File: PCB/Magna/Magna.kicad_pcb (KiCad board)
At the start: 2 copper layers, 100 x 100 mm, 136 parts, among them J702 Conn_ARM_SWD_TagConnect_TC2030, J703 Conn_ARM_JTAG_SWD_20, U1001 6N137, U1002 74HC08D, U201 24.576 MHz, U202 CY2305SXC-1HT, U203 CY2305SXC-1HT, U301 WM8782SEDS, U401 WM8782SEDS, U501 CS4344, U601 CS4344, U701 STM32F730V8T6, U802 USB3300-EZK, U901 AMS1117-5.0, U902 WS3222D, U903 TPS61040DBV, U904 XL1509-ADJ, Y701 24MHz

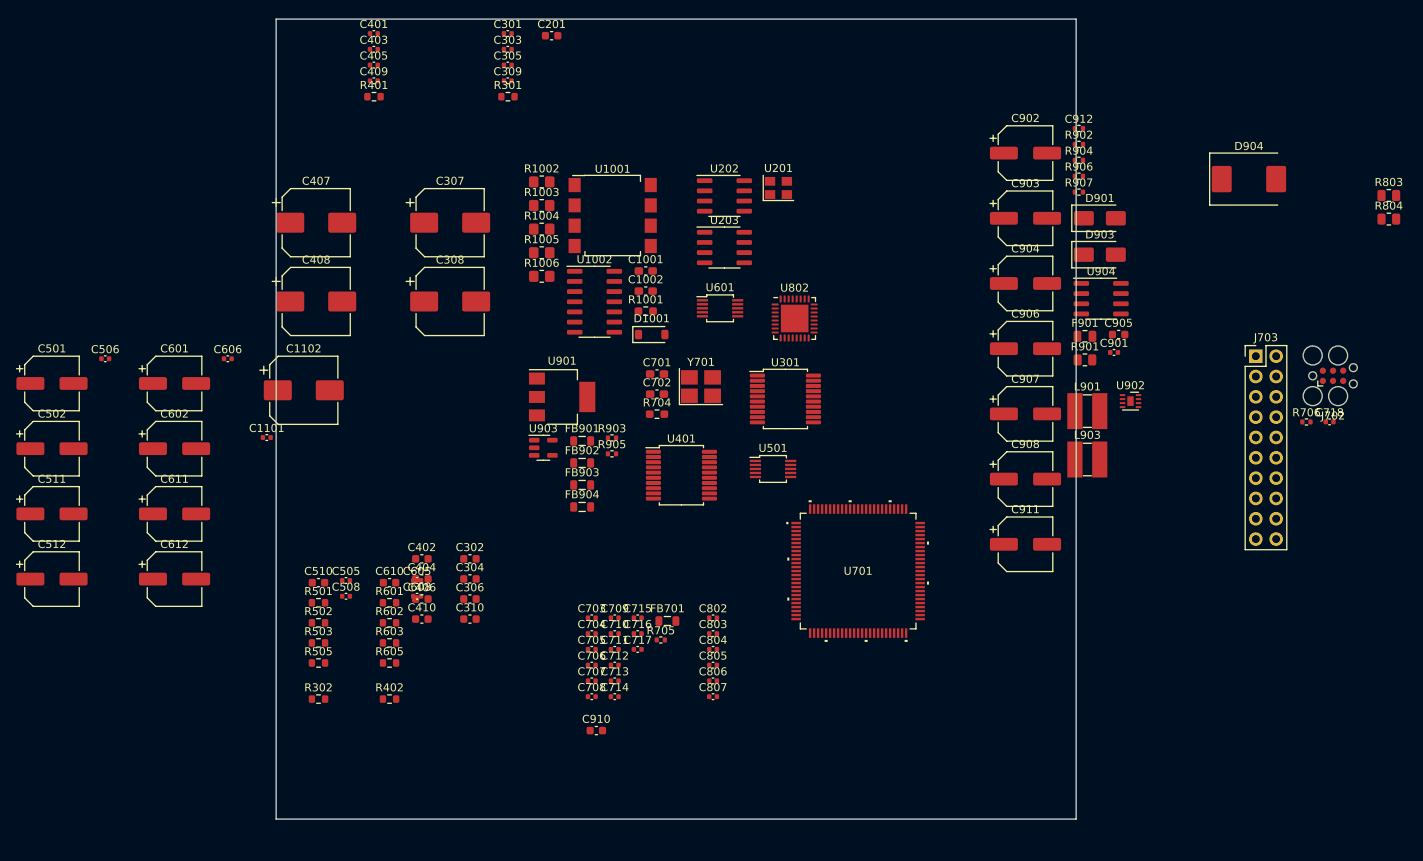
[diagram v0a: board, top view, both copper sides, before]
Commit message: Remove all ERC in schematics
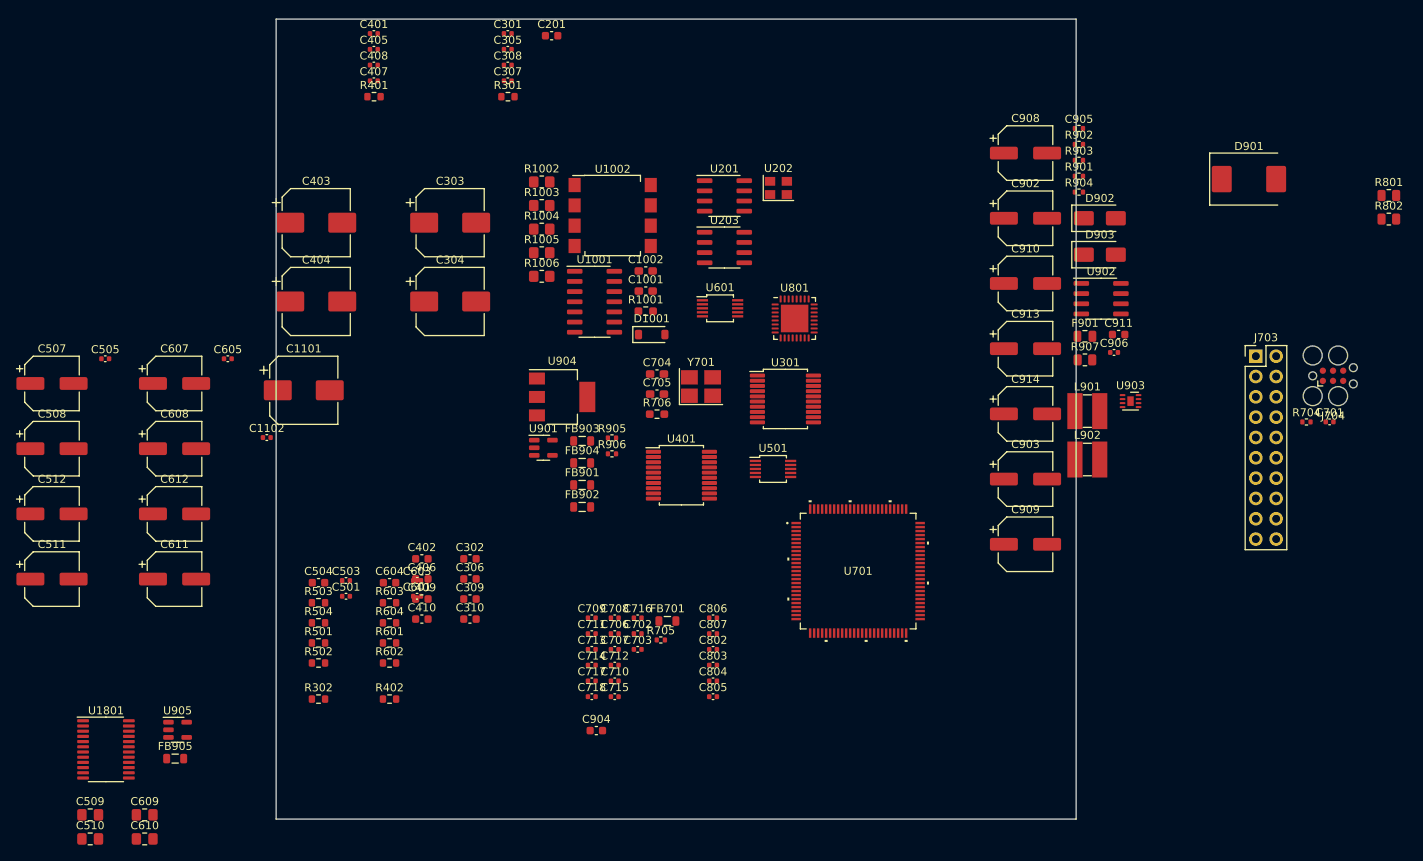
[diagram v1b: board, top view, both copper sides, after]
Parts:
- added C509: 10nF/50V, Capacitor_SMD:C_0805_2012Metric_Pad1.18x1.45mm_HandSolder, F.Cu at (46.8, 154.5)
- added C510: 10nF/50V, Capacitor_SMD:C_0805_2012Metric_Pad1.18x1.45mm_HandSolder, F.Cu at (46.8, 157.5)
- added C609: 10nF/50V, Capacitor_SMD:C_0805_2012Metric_Pad1.18x1.45mm_HandSolder, F.Cu at (53.6, 154.5)
- added C610: 10nF/50V, Capacitor_SMD:C_0805_2012Metric_Pad1.18x1.45mm_HandSolder, F.Cu at (53.6, 157.5)
- added FB905: FerriteBead, Inductor_SMD:L_0805_2012Metric, F.Cu at (57.4, 147.4)
- added U1801: XL9535, Package_SO:TSSOP-24_4.4x7.8mm_P0.65mm, F.Cu at (48.7, 146.3)
- added U905: AP2171W, Package_TO_SOT_SMD:SOT-23-5, F.Cu at (57.7, 143.8)
- renumbered C1002 to C1001, C1001 to C1002, C1102 to C1101, C1101 to C1102, C307 to C303, C308 to C304, C303 to C305, C304 to C306, C309 to C307, C305 to C308, C306 to C309, C407 to C403, C408 to C404, C403 to C405, C404 to C406, C409 to C407, C405 to C408, C406 to C409, C508 to C501, C505 to C503, C510 to C504, C506 to C505, C501 to C507, C502 to C508, C512 to C511, C511 to C512, C608 to C601, C605 to C603, C610 to C604, C606 to C605, C601 to C607, C602 to C608, C612 to C611, C611 to C612, C718 to C701, C716 to C702, C717 to C703, C701 to C704, C702 to C705, C710 to C706, C711 to C707, C709 to C708, C703 to C709, C713 to C710, C704 to C711, C705 to C713, C706 to C714, C714 to C715, C715 to C716, C707 to C717, C708 to C718, C804 to C802, C805 to C803, C806 to C804, C807 to C805, C802 to C806, C803 to C807, C903 to C902, C908 to C903, C910 to C904, C912 to C905, C901 to C906, C902 to C908, C911 to C909, C904 to C910, C905 to C911, C906 to C913, C907 to C914, D904 to D901, D901 to D902, FB903 to FB901, FB904 to FB902, FB901 to FB903, FB902 to FB904, J702 to J704, L903 to L902, R503 to R501, R505 to R502, R501 to R503, R502 to R504, R603 to R601, R605 to R602, R601 to R603, R602 to R604, R706 to R704, R704 to R706, R803 to R801, R804 to R802, R906 to R901, R904 to R903, R907 to R904, R903 to R905, R905 to R906, R901 to R907, U1002 to U1001, U1001 to U1002, U202 to U201, U201 to U202, U802 to U801, U903 to U901, U904 to U902, U902 to U903, U901 to U904
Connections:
- net /MCU/MCU_VDDA renamed VDDA
- net /POWER/~{HSW_EN} renamed /MCU/~{HSW_EN}
- U901 pad 4: /POWER/Boost in -> /MCU/VA_en

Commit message: Select parts for all components
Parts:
- added C1201: 100u/10V, Capacitor_SMD:CP_Elec_6.3x5.8, F.Cu at (327.5, 32.8)
- added C1202: 100u/10V, Capacitor_SMD:CP_Elec_6.3x5.8, F.Cu at (327.5, 41.0)
- added C1203: 22uF/16V, Capacitor_SMD:CP_Elec_5x5.8, F.Cu at (351.3, 55.8)
- added C1204: 22uF/16V, Capacitor_SMD:CP_Elec_5x5.8, F.Cu at (351.3, 62.6)
- added C1205: 100pF/50V, Capacitor_SMD:C_0805_2012Metric, F.Cu at (339.7, 30.3)
- added C1206: 100pF/50V, Capacitor_SMD:C_0805_2012Metric, F.Cu at (339.7, 33.3)
- added C1207: 220uF, Capacitor_SMD:CP_Elec_4x5.8, F.Cu at (350.2, 31.7)
- added C1208: 220uF, Capacitor_SMD:CP_Elec_4x5.8, F.Cu at (350.2, 37.5)
- added C1209: 100u/10V, Capacitor_SMD:CP_Elec_6.3x5.8, F.Cu at (327.5, 49.1)
- added C1210: 100u/10V, Capacitor_SMD:CP_Elec_6.3x5.8, F.Cu at (327.5, 57.3)
- added C1211: 100nF/16V, Capacitor_SMD:C_0805_2012Metric, F.Cu at (339.7, 36.3)
- added C1212: 10uF/25V, Capacitor_SMD:CP_Elec_4x5.8, F.Cu at (350.2, 43.4)
- added C1213: 100nF/16V, Capacitor_SMD:C_0805_2012Metric, F.Cu at (339.7, 39.3)
- added C1214: 100u/10V, Capacitor_SMD:CP_Elec_6.3x5.8, F.Cu at (327.5, 65.4)
- added C1215: 100u/10V, Capacitor_SMD:CP_Elec_6.3x5.8, F.Cu at (327.5, 73.6)
- added C1216: 100nF/16V, Capacitor_SMD:C_0805_2012Metric, F.Cu at (339.7, 42.3)
- added C1217: 100nF/16V, Capacitor_SMD:C_0805_2012Metric, F.Cu at (339.7, 45.3)
- added C1301: 100u/10V, Capacitor_SMD:CP_Elec_6.3x5.8, F.Cu at (317.3, 122.3)
- added C1302: 100u/10V, Capacitor_SMD:CP_Elec_6.3x5.8, F.Cu at (317.3, 130.5)
- added C1303: 100nF/16V, Capacitor_SMD:C_0805_2012Metric, F.Cu at (324.7, 131.6)
- added C1304: 22uF/16V, Capacitor_SMD:CP_Elec_5x5.8, F.Cu at (331.4, 133.5)
- added C1305: 22uF/16V, Capacitor_SMD:CP_Elec_5x5.8, F.Cu at (331.4, 140.3)
- added C1306: 100nF/16V, Capacitor_SMD:C_0805_2012Metric, F.Cu at (324.7, 134.6)
- added C1307: 100nF/16V, Capacitor_SMD:C_0805_2012Metric, F.Cu at (324.7, 137.6)
- added C1308: 100pF/50V, Capacitor_SMD:C_0805_2012Metric, F.Cu at (324.7, 140.6)
- added C1309: 100pF/50V, Capacitor_SMD:C_0805_2012Metric, F.Cu at (324.7, 143.6)
- added C1310: 220uF, Capacitor_SMD:CP_Elec_4x5.8, F.Cu at (340.6, 121.2)
- added C1311: 220uF, Capacitor_SMD:CP_Elec_4x5.8, F.Cu at (340.6, 127.0)
- added C1312: 47p/50V, Capacitor_SMD:C_0805_2012Metric, F.Cu at (324.7, 146.6)
- added C1313: 47p/50V, Capacitor_SMD:C_0805_2012Metric, F.Cu at (324.7, 149.6)
- added C1314: 100u/10V, Capacitor_SMD:CP_Elec_6.3x5.8, F.Cu at (317.3, 138.6)
- added C1315: 100u/10V, Capacitor_SMD:CP_Elec_6.3x5.8, F.Cu at (317.3, 146.8)
- added C1501: 100nF/16V, Capacitor_SMD:C_0805_2012Metric, F.Cu at (368.5, 30.3)
- added C1601: 100nF/16V, Capacitor_SMD:C_0805_2012Metric, F.Cu at (357.2, 134.6)
- added C1701: 100nF/16V, Capacitor_SMD:C_0805_2012Metric, F.Cu at (368.5, 43.7)
- added C1801: 100nF/16V, Capacitor_SMD:C_0805_2012Metric, F.Cu at (314.3, 82.4)
- added C1802: 100nF/16V, Capacitor_SMD:C_0805_2012Metric, F.Cu at (314.3, 85.4)
- added C1803: 100nF/16V, Capacitor_SMD:C_0805_2012Metric, F.Cu at (314.3, 88.4)
- added C1804: 100nF/16V, Capacitor_SMD:C_0805_2012Metric, F.Cu at (314.3, 91.4)
- added C1805: 100nF/16V, Capacitor_SMD:C_0805_2012Metric, F.Cu at (314.3, 94.4)
- added C1806: 100nF/16V, Capacitor_SMD:C_0805_2012Metric, F.Cu at (314.3, 97.4)
- added C1807: 100nF/16V, Capacitor_SMD:C_0805_2012Metric, F.Cu at (318.7, 82.4)
- added C1808: 100nF/16V, Capacitor_SMD:C_0805_2012Metric, F.Cu at (318.7, 85.4)
- added C1809: 100nF/16V, Capacitor_SMD:C_0805_2012Metric, F.Cu at (318.7, 88.4)
- added C1810: 100nF/16V, Capacitor_SMD:C_0805_2012Metric, F.Cu at (318.7, 91.4)
- added C1811: 100nF/16V, Capacitor_SMD:C_0805_2012Metric, F.Cu at (318.7, 94.4)
- added C1812: 100nF/16V, Capacitor_SMD:C_0805_2012Metric, F.Cu at (318.7, 97.4)
- added C1813: 100nF/16V, Capacitor_SMD:C_0805_2012Metric, F.Cu at (323.2, 82.4)
- added C1814: 100nF/16V, Capacitor_SMD:C_0805_2012Metric, F.Cu at (323.2, 85.4)
- added C1815: 100nF/16V, Capacitor_SMD:C_0805_2012Metric, F.Cu at (323.2, 88.4)
- added C1816: 100nF/16V, Capacitor_SMD:C_0805_2012Metric, F.Cu at (323.2, 91.4)
- added C1817: 100nF/16V, Capacitor_SMD:C_0805_2012Metric, F.Cu at (323.2, 94.4)
- added C2001: 100nF/16V, Capacitor_SMD:C_0805_2012Metric, F.Cu at (298.8, 65.3)
- added C2002: 100nF/16V, Capacitor_SMD:C_0805_2012Metric, F.Cu at (298.8, 68.3)
- added C2003: 100nF/16V, Capacitor_SMD:C_0805_2012Metric, F.Cu at (298.8, 71.3)
- added C2004: 100nF/16V, Capacitor_SMD:C_0805_2012Metric, F.Cu at (298.8, 74.3)
- added C2005: 100nF/16V, Capacitor_SMD:C_0805_2012Metric, F.Cu at (298.8, 77.3)
- added C301: 10uF/25V, Capacitor_SMD:CP_Elec_4x5.8, F.Cu at (252.3, 93.7)
- added C302: 10uF/25V, Capacitor_SMD:CP_Elec_4x5.8, F.Cu at (252.3, 99.6)
- added C304: 10uF/25V, Capacitor_SMD:CP_Elec_4x5.8, F.Cu at (252.3, 105.4)
- added C307: 10uF/25V, Capacitor_SMD:CP_Elec_4x5.8, F.Cu at (252.3, 111.3)
- added C309: 10uF/25V, Capacitor_SMD:CP_Elec_4x5.8, F.Cu at (252.3, 117.1)
- added C310: 10uF/25V, Capacitor_SMD:CP_Elec_4x5.8, F.Cu at (252.3, 123.0)
- added C401: 10uF/25V, Capacitor_SMD:CP_Elec_4x5.8, F.Cu at (345.5, 83.8)
- added C402: 10uF/25V, Capacitor_SMD:CP_Elec_4x5.8, F.Cu at (345.5, 89.6)
- added C404: 10uF/25V, Capacitor_SMD:CP_Elec_4x5.8, F.Cu at (345.5, 95.5)
- added C407: 10uF/25V, Capacitor_SMD:CP_Elec_4x5.8, F.Cu at (345.5, 101.3)
- added C409: 10uF/25V, Capacitor_SMD:CP_Elec_4x5.8, F.Cu at (345.5, 107.2)
- added C410: 10uF/25V, Capacitor_SMD:CP_Elec_4x5.8, F.Cu at (345.5, 113.0)
- added C502: 1uF/50V, Capacitor_SMD:C_0805_2012Metric, F.Cu at (368.4, 88.3)
- added C504: 10uF/25V, Capacitor_SMD:CP_Elec_4x5.8, F.Cu at (362.3, 83.8)
- added C505: 10uF/25V, Capacitor_SMD:CP_Elec_4x5.8, F.Cu at (362.3, 89.6)
- added C602: 1uF/50V, Capacitor_SMD:C_0805_2012Metric, F.Cu at (367.8, 63.1)
- added C604: 10uF/25V, Capacitor_SMD:CP_Elec_4x5.8, F.Cu at (361.7, 58.6)
- added C605: 10uF/25V, Capacitor_SMD:CP_Elec_4x5.8, F.Cu at (361.7, 64.4)
- added C801: 100nF/16V, Capacitor_SMD:C_0805_2012Metric, F.Cu at (297.8, 100.0)
- added C802: 100nF/16V, Capacitor_SMD:C_0805_2012Metric, F.Cu at (297.8, 103.0)
- added C803: 220uF, Capacitor_SMD:CP_Elec_4x5.8, F.Cu at (300.1, 93.9)
- added C804: 100nF/16V, Capacitor_SMD:C_0805_2012Metric, F.Cu at (297.8, 106.0)
- added C805: 100nF/16V, Capacitor_SMD:C_0805_2012Metric, F.Cu at (297.8, 109.0)
- added C901: 10uF/25V, Capacitor_SMD:CP_Elec_4x5.8, F.Cu at (354.8, 128.2)
- added C907: 22pF/50V, Capacitor_SMD:C_0805_2012Metric, F.Cu at (348.7, 119.8)
- added C912: 100nF/16V, Capacitor_SMD:C_0805_2012Metric, F.Cu at (348.7, 122.8)
- added C915: 100nF/16V, Capacitor_SMD:C_0805_2012Metric, F.Cu at (348.7, 125.8)
- added D2001: Red, Diode_SMD:D_0805_2012Metric_Pad1.15x1.40mm_HandSolder, F.Cu at (275.0, 41.7)
- added D2002: yellow, Diode_SMD:D_0805_2012Metric_Pad1.15x1.40mm_HandSolder, F.Cu at (275.0, 44.8)
- added D2003: yellow, Diode_SMD:D_0805_2012Metric_Pad1.15x1.40mm_HandSolder, F.Cu at (275.0, 47.8)
- added D2004: yellow, Diode_SMD:D_0805_2012Metric_Pad1.15x1.40mm_HandSolder, F.Cu at (275.0, 50.8)
- added D2005: green, Diode_SMD:D_0805_2012Metric_Pad1.15x1.40mm_HandSolder, F.Cu at (275.0, 53.9)
- added D2006: green, Diode_SMD:D_0805_2012Metric_Pad1.15x1.40mm_HandSolder, F.Cu at (275.0, 56.9)
- added D2007: green, Diode_SMD:D_0805_2012Metric_Pad1.15x1.40mm_HandSolder, F.Cu at (275.0, 60.0)
- added D2008: green, Diode_SMD:D_0805_2012Metric_Pad1.15x1.40mm_HandSolder, F.Cu at (275.0, 63.0)
- added D2009: Red, Diode_SMD:D_0805_2012Metric_Pad1.15x1.40mm_HandSolder, F.Cu at (275.0, 66.0)
- added D2010: yellow, Diode_SMD:D_0805_2012Metric_Pad1.15x1.40mm_HandSolder, F.Cu at (279.8, 41.7)
- added D2011: yellow, Diode_SMD:D_0805_2012Metric_Pad1.15x1.40mm_HandSolder, F.Cu at (279.8, 44.8)
- added D2012: yellow, Diode_SMD:D_0805_2012Metric_Pad1.15x1.40mm_HandSolder, F.Cu at (279.8, 47.8)
- added D2013: green, Diode_SMD:D_0805_2012Metric_Pad1.15x1.40mm_HandSolder, F.Cu at (279.8, 50.8)
- added D2014: green, Diode_SMD:D_0805_2012Metric_Pad1.15x1.40mm_HandSolder, F.Cu at (279.8, 53.9)
- added D2015: green, Diode_SMD:D_0805_2012Metric_Pad1.15x1.40mm_HandSolder, F.Cu at (279.8, 56.9)
- added D2016: green, Diode_SMD:D_0805_2012Metric_Pad1.15x1.40mm_HandSolder, F.Cu at (279.8, 60.0)
- added D2017: Red, Diode_SMD:D_0805_2012Metric_Pad1.15x1.40mm_HandSolder, F.Cu at (279.8, 63.0)
- added D2018: yellow, Diode_SMD:D_0805_2012Metric_Pad1.15x1.40mm_HandSolder, F.Cu at (279.8, 66.0)
- added D2019: yellow, Diode_SMD:D_0805_2012Metric_Pad1.15x1.40mm_HandSolder, F.Cu at (284.6, 41.7)
- added D2020: yellow, Diode_SMD:D_0805_2012Metric_Pad1.15x1.40mm_HandSolder, F.Cu at (284.6, 44.8)
- added D2021: green, Diode_SMD:D_0805_2012Metric_Pad1.15x1.40mm_HandSolder, F.Cu at (284.6, 47.8)
- added D2022: green, Diode_SMD:D_0805_2012Metric_Pad1.15x1.40mm_HandSolder, F.Cu at (284.6, 50.8)
- added D2023: green, Diode_SMD:D_0805_2012Metric_Pad1.15x1.40mm_HandSolder, F.Cu at (284.6, 53.9)
- added D2024: green, Diode_SMD:D_0805_2012Metric_Pad1.15x1.40mm_HandSolder, F.Cu at (284.6, 56.9)
- added D2025: yellow, Diode_SMD:D_0805_2012Metric_Pad1.15x1.40mm_HandSolder, F.Cu at (284.6, 60.0)
- added D2026: White, Diode_SMD:D_0805_2012Metric_Pad1.15x1.40mm_HandSolder, F.Cu at (284.6, 63.0)
- added D2027: White, Diode_SMD:D_0805_2012Metric_Pad1.15x1.40mm_HandSolder, F.Cu at (284.6, 66.0)
- added D2028: yellow, Diode_SMD:D_0805_2012Metric_Pad1.15x1.40mm_HandSolder, F.Cu at (289.4, 41.7)
- added D2029: green, Diode_SMD:D_0805_2012Metric_Pad1.15x1.40mm_HandSolder, F.Cu at (289.4, 44.8)
- added D2030: green, Diode_SMD:D_0805_2012Metric_Pad1.15x1.40mm_HandSolder, F.Cu at (289.4, 47.8)
- added D2031: yellow, Diode_SMD:D_0805_2012Metric_Pad1.15x1.40mm_HandSolder, F.Cu at (289.4, 50.8)
- added D2032: White, Diode_SMD:D_0805_2012Metric_Pad1.15x1.40mm_HandSolder, F.Cu at (289.4, 53.9)
- added D2033: White, Diode_SMD:D_0805_2012Metric_Pad1.15x1.40mm_HandSolder, F.Cu at (289.4, 56.9)
- added D2034: green, Diode_SMD:D_0805_2012Metric_Pad1.15x1.40mm_HandSolder, F.Cu at (289.4, 60.0)
- added D2035: green, Diode_SMD:D_0805_2012Metric_Pad1.15x1.40mm_HandSolder, F.Cu at (289.4, 63.0)
- added D2036: green, Diode_SMD:D_0805_2012Metric_Pad1.15x1.40mm_HandSolder, F.Cu at (289.4, 66.0)
- added D2037: yellow, Diode_SMD:D_0805_2012Metric_Pad1.15x1.40mm_HandSolder, F.Cu at (294.2, 41.7)
- added D2038: yellow, Diode_SMD:D_0805_2012Metric_Pad1.15x1.40mm_HandSolder, F.Cu at (294.2, 44.8)
- added D2039: White, Diode_SMD:D_0805_2012Metric_Pad1.15x1.40mm_HandSolder, F.Cu at (294.2, 47.8)
- added D2040: Red, Diode_SMD:D_0805_2012Metric_Pad1.15x1.40mm_HandSolder, F.Cu at (294.2, 50.8)
- added D2101: Red, Diode_SMD:D_0805_2012Metric_Pad1.15x1.40mm_HandSolder, F.Cu at (301.6, 119.8)
- added D2102: Red, Diode_SMD:D_0805_2012Metric_Pad1.15x1.40mm_HandSolder, F.Cu at (301.6, 122.8)
- added D2103: Red, Diode_SMD:D_0805_2012Metric_Pad1.15x1.40mm_HandSolder, F.Cu at (301.6, 125.9)
- added D2104: Red, Diode_SMD:D_0805_2012Metric_Pad1.15x1.40mm_HandSolder, F.Cu at (301.6, 128.9)
- added D2105: Red, Diode_SMD:D_0805_2012Metric_Pad1.15x1.40mm_HandSolder, F.Cu at (301.6, 131.9)
- added D2106: Red, Diode_SMD:D_0805_2012Metric_Pad1.15x1.40mm_HandSolder, F.Cu at (301.6, 135.0)
- added D2107: Red, Diode_SMD:D_0805_2012Metric_Pad1.15x1.40mm_HandSolder, F.Cu at (301.6, 138.0)
- added D801: SS54, Diode_SMD:D_SMA_Handsoldering, F.Cu at (305.0, 100.7)
- added D802: SS54, Diode_SMD:D_SMA_Handsoldering, F.Cu at (305.0, 105.3)
- added D805: green, Diode_SMD:D_0805_2012Metric_Pad1.15x1.40mm_HandSolder, F.Cu at (306.4, 92.5)
- added D806: green, Diode_SMD:D_0805_2012Metric_Pad1.15x1.40mm_HandSolder, F.Cu at (306.4, 95.5)
- added F902: 300mA, Fuse:Fuse_2920_7451Metric_Pad2.10x5.45mm_HandSolder, F.Cu at (356.3, 121.8)
- added J1001: DIN-5_180degree, Skrooter_footprints:DIN-504-M10, F.Cu at (259.5, 41.6)
- added J1002: DIN-5_180degree, Skrooter_footprints:DIN-504-M10, F.Cu at (259.5, 61.6)
- added J1003: DIN-5_180degree, Skrooter_footprints:DIN-504-M10, F.Cu at (259.5, 81.7)
- added J1201: AudioJack3, Connector_Audio:Jack_3.5mm_CUI_SJ1-3525N_Horizontal, F.Cu at (339.8, 60.8)
- added J702: Conn_02x06_Odd_Even, Connector_PinSocket_2.54mm:PinSocket_2x06_P2.54mm_Vertical_SMD, F.Cu at (282.1, 126.9)
- added J705: Boot Jumper, Connector_PinHeader_2.54mm:PinHeader_1x03_P2.54mm_Vertical, F.Cu at (279.3, 137.9)
- added J706: Conn_02x06_Odd_Even, Connector_PinSocket_2.54mm:PinSocket_2x06_P2.54mm_Vertical_SMD, F.Cu at (292.2, 126.9)
- added J801: USB_A, Connector_USB:USB_A_Molex_67643_Horizontal, F.Cu at (282.9, 101.7)
- added J802: USB_C_Receptacle_USB2.0, Connector_USB:USB_C_Receptacle_G-Switch_GT-USB-7010ASV, F.Cu at (302.1, 86.2)
- added J803: USB_B, Connector_USB:USB_B_OST_USB-B1HSxx_Horizontal, F.Cu at (280.2, 88.4)
- added JP201: Jumper_2_Open, Jumper:SolderJumper-2_P1.3mm_Open_TrianglePad1.0x1.5mm, F.Cu at (250.6, 129.7)
- added JP202: Jumper_2_Open, Jumper:SolderJumper-2_P1.3mm_Open_TrianglePad1.0x1.5mm, F.Cu at (250.6, 133.2)
- added JP203: Jumper_2_Open, Jumper:SolderJumper-2_P1.3mm_Open_TrianglePad1.0x1.5mm, F.Cu at (250.6, 136.8)
- added JP204: Jumper_2_Open, Jumper:SolderJumper-2_P1.3mm_Open_TrianglePad1.0x1.5mm, F.Cu at (250.6, 140.3)
- added JP205: Jumper_2_Open, Jumper:SolderJumper-2_P1.3mm_Open_TrianglePad1.0x1.5mm, F.Cu at (250.6, 143.9)
- added JP206: Jumper_2_Open, Jumper:SolderJumper-2_P1.3mm_Open_TrianglePad1.0x1.5mm, F.Cu at (255.0, 129.7)
- added JP207: Jumper_2_Open, Jumper:SolderJumper-2_P1.3mm_Open_TrianglePad1.0x1.5mm, F.Cu at (255.0, 133.2)
- added JP208: Jumper_2_Open, Jumper:SolderJumper-2_P1.3mm_Open_TrianglePad1.0x1.5mm, F.Cu at (255.0, 136.8)
- added JP209: Jumper_2_Open, Jumper:SolderJumper-2_P1.3mm_Open_TrianglePad1.0x1.5mm, F.Cu at (255.0, 140.3)
- added JP210: Jumper_2_Open, Jumper:SolderJumper-2_P1.3mm_Open_TrianglePad1.0x1.5mm, F.Cu at (255.0, 143.9)
- added JP301: SolderJumper_3_Bridged12, Jumper:SolderJumper-3_P2.0mm_Open_TrianglePad1.0x1.5mm_NumberLabels, F.Cu at (259.7, 92.6)
- added JP302: SolderJumper_3_Bridged12, Jumper:SolderJumper-3_P2.0mm_Open_TrianglePad1.0x1.5mm_NumberLabels, F.Cu at (259.7, 96.2)
- added JP303: SolderJumper_3_Bridged12, Jumper:SolderJumper-3_P2.0mm_Open_TrianglePad1.0x1.5mm_NumberLabels, F.Cu at (259.7, 99.8)
- added JP304: SolderJumper_3_Bridged12, Jumper:SolderJumper-3_P2.0mm_Open_TrianglePad1.0x1.5mm_NumberLabels, F.Cu at (259.7, 103.3)
- added JP401: SolderJumper_3_Bridged12, Jumper:SolderJumper-3_P2.0mm_Open_TrianglePad1.0x1.5mm_NumberLabels, F.Cu at (352.9, 82.7)
- added JP402: SolderJumper_3_Bridged12, Jumper:SolderJumper-3_P2.0mm_Open_TrianglePad1.0x1.5mm_NumberLabels, F.Cu at (352.9, 86.2)
- added JP403: SolderJumper_3_Bridged12, Jumper:SolderJumper-3_P2.0mm_Open_TrianglePad1.0x1.5mm_NumberLabels, F.Cu at (352.9, 89.8)
- added JP404: SolderJumper_3_Bridged12, Jumper:SolderJumper-3_P2.0mm_Open_TrianglePad1.0x1.5mm_NumberLabels, F.Cu at (352.9, 93.4)
- added R1101: 22k, Resistor_SMD:R_0805_2012Metric, F.Cu at (360.6, 96.0)
- added R1102: 22k, Resistor_SMD:R_0805_2012Metric, F.Cu at (360.6, 99.0)
- added R1201: 22k, Resistor_SMD:R_0805_2012Metric, F.Cu at (344.1, 30.2)
- added R1202: 22k, Resistor_SMD:R_0805_2012Metric, F.Cu at (344.1, 33.2)
- added R1203: 680R, Resistor_SMD:R_0805_2012Metric_Pad1.20x1.40mm_HandSolder, F.Cu at (335.1, 30.2)
- added R1204: 680R, Resistor_SMD:R_0805_2012Metric_Pad1.20x1.40mm_HandSolder, F.Cu at (335.1, 33.2)
- added R1205: 1k3, Resistor_SMD:R_0805_2012Metric_Pad1.20x1.40mm_HandSolder, F.Cu at (335.1, 36.1)
- added R1206: 1k3, Resistor_SMD:R_0805_2012Metric_Pad1.20x1.40mm_HandSolder, F.Cu at (335.1, 39.1)
- added R1207: 22k, Resistor_SMD:R_0805_2012Metric, F.Cu at (344.1, 36.1)
- added R1208: 22k, Resistor_SMD:R_0805_2012Metric, F.Cu at (344.1, 39.1)
- added R1209: 100R, Resistor_SMD:R_0805_2012Metric_Pad1.20x1.40mm_HandSolder, F.Cu at (335.1, 42.0)
- added R1210: 100R, Resistor_SMD:R_0805_2012Metric_Pad1.20x1.40mm_HandSolder, F.Cu at (335.1, 45.0)
- added R1211: 10k, Resistor_SMD:R_0805_2012Metric, F.Cu at (344.1, 42.0)
- added R1212: 10k, Resistor_SMD:R_0805_2012Metric, F.Cu at (344.1, 45.0)
- added R1213: 4R7, Resistor_SMD:R_0805_2012Metric_Pad1.20x1.40mm_HandSolder, F.Cu at (335.1, 47.9)
- added R1214: 4R7, Resistor_SMD:R_0805_2012Metric_Pad1.20x1.40mm_HandSolder, F.Cu at (335.1, 50.9)
- added R1301: 22k, Resistor_SMD:R_0805_2012Metric, F.Cu at (338.1, 131.5)
- added R1302: 22k, Resistor_SMD:R_0805_2012Metric, F.Cu at (338.1, 134.5)
- added R1303: 680R, Resistor_SMD:R_0805_2012Metric_Pad1.20x1.40mm_HandSolder, F.Cu at (324.9, 119.7)
- added R1304: 680R, Resistor_SMD:R_0805_2012Metric_Pad1.20x1.40mm_HandSolder, F.Cu at (324.9, 122.7)
- added R1305: 1k3, Resistor_SMD:R_0805_2012Metric_Pad1.20x1.40mm_HandSolder, F.Cu at (324.9, 125.6)
- added R1306: 1k3, Resistor_SMD:R_0805_2012Metric_Pad1.20x1.40mm_HandSolder, F.Cu at (324.9, 128.6)
- added R1307: 22k, Resistor_SMD:R_0805_2012Metric, F.Cu at (338.1, 137.4)
- added R1308: 22k, Resistor_SMD:R_0805_2012Metric, F.Cu at (338.1, 140.4)
- added R1309: 100R, Resistor_SMD:R_0805_2012Metric_Pad1.20x1.40mm_HandSolder, F.Cu at (329.6, 119.7)
- added R1310: 100R, Resistor_SMD:R_0805_2012Metric_Pad1.20x1.40mm_HandSolder, F.Cu at (329.6, 122.7)
- added R1311: 4k7, Resistor_SMD:R_0805_2012Metric_Pad1.20x1.40mm_HandSolder, F.Cu at (329.6, 125.6)
- added R1312: 4k7, Resistor_SMD:R_0805_2012Metric_Pad1.20x1.40mm_HandSolder, F.Cu at (329.6, 128.6)
- added R1313: 4k7, Resistor_SMD:R_0805_2012Metric_Pad1.20x1.40mm_HandSolder, F.Cu at (334.4, 119.7)
- added R1314: 4k7, Resistor_SMD:R_0805_2012Metric_Pad1.20x1.40mm_HandSolder, F.Cu at (334.4, 122.7)
- added R1315: 68R, Resistor_SMD:R_0805_2012Metric_Pad1.20x1.40mm_HandSolder, F.Cu at (334.4, 125.6)
- added R1316: 68R, Resistor_SMD:R_0805_2012Metric_Pad1.20x1.40mm_HandSolder, F.Cu at (334.4, 128.6)
- added R1317: 22k, Resistor_SMD:R_0805_2012Metric, F.Cu at (338.1, 143.3)
- added R1318: 22k, Resistor_SMD:R_0805_2012Metric, F.Cu at (338.1, 146.3)
- added R1801: 10k, Resistor_SMD:R_0805_2012Metric, F.Cu at (327.6, 82.3)
- added R1802: 10k, Resistor_SMD:R_0805_2012Metric, F.Cu at (327.6, 85.3)
- added R1803: 10k, Resistor_SMD:R_0805_2012Metric, F.Cu at (327.6, 88.2)
- added R1804: 10k, Resistor_SMD:R_0805_2012Metric, F.Cu at (327.6, 91.2)
- added R1805: 10k, Resistor_SMD:R_0805_2012Metric, F.Cu at (327.6, 94.1)
- added R1806: 1k, Resistor_SMD:R_0805_2012Metric_Pad1.20x1.40mm_HandSolder, F.Cu at (327.8, 100.0)
- added R1807: 1k, Resistor_SMD:R_0805_2012Metric_Pad1.20x1.40mm_HandSolder, F.Cu at (327.8, 103.0)
- added R1808: 1k, Resistor_SMD:R_0805_2012Metric_Pad1.20x1.40mm_HandSolder, F.Cu at (327.8, 105.9)
- added R1809: 1k, Resistor_SMD:R_0805_2012Metric_Pad1.20x1.40mm_HandSolder, F.Cu at (327.8, 108.9)
- added R1810: 10k, Resistor_SMD:R_0805_2012Metric, F.Cu at (327.6, 97.1)
- added R1811: 10k, Resistor_SMD:R_0805_2012Metric, F.Cu at (332.0, 82.3)
- renumbered C704 to C717, C705 to C718, J704 to J703, R801 to R811, R802 to R812, U203 to U202, U201 to U203, U801 to U802
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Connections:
- C1002 pad 2: +3.3V -> VDD
- C717 pad 2: /MCU/XTAL_{IN} -> /MCU/OSC_{IN}
- C806 pad 1: /USB/USB_VDD_1.8 -> /USB/USB_VDDA_1.8
- J704 pad 10: GND -> /MCU/MCU_NRST
- J704 pad 2: VDD -> /MCU/JTMS_SWDIO
- J704 pad 3: /MCU/NJTRST -> GND
- J704 pad 4: GND -> /MCU/JTCK_SWCLK
- J704 pad 5: /MCU/JTDI -> GND
- J704 pad 6: GND -> /MCU/JTDO_SWO
- J704 pad 7: /MCU/JTMS_SWDIO -> unconnected-(J704-KEY-Pad7)
- J704 pad 8: GND -> /MCU/JTDI
- J704 pad 9: /MCU/JTCK_SWCLK -> GND
- R1001 pad 2: +3.3V -> VDD
- R301 pad 2: Net-(C303-Pad1) -> Net-(C301-Pad1)
- R302 pad 2: Net-(C304-Pad1) -> Net-(C302-Pad1)
- R401 pad 2: Net-(C403-Pad1) -> Net-(C401-Pad1)
- R402 pad 2: Net-(C404-Pad1) -> Net-(C402-Pad1)
- R811 pad 1: /USB/USBA_CON_CC1 -> /USB/USB_C_CON_CC1
- R812 pad 1: /USB/USBA_CON_CC2 -> /USB/USB_C_CON_CC2
- U1002 pad 4: (no net) -> unconnected-(U1002-NC-Pad4)
- U1002 pad 8: +3.3V -> VDD
- U201 pad 1: GND -> Net-(U201-Tri-State)
- U203 pad 8: /Audio IO/BCLK_BUF -> Net-(JP206-A)
- U301 pad 20: /Audio IO/ADC_M/S -> /Audio IO/ADC_CONFIG.ADC_M/S
- U701 pad 1: (no net) -> /MCU/~{HSW_EN}
- U701 pad 10: (no net) -> GND
- U701 pad 100: (no net) -> VDD
- U701 pad 11: (no net) -> VDD
- U701 pad 12: (no net) -> /MCU/OSC_{IN}
- U701 pad 13: (no net) -> /MCU/OSC_{OUT}
- U701 pad 14: (no net) -> /MCU/MCU_NRST
- U701 pad 15: (no net) -> /MCU/STP
- U701 pad 16: (no net) -> /Human Interface/ADC_4
- U701 pad 17: (no net) -> /MCU/DIR
- U701 pad 18: (no net) -> /MCU/NXT
- U701 pad 19: (no net) -> GND
- U701 pad 2: (no net) -> /Audio IO/ADCIN1
- U701 pad 20: (no net) -> /MCU/MCU_VREF+
- U701 pad 21: (no net) -> VDDA
- U701 pad 22: (no net) -> /Human Interface/ADC_0
- U701 pad 23: (no net) -> /Human Interface/ADC_1
- U701 pad 24: (no net) -> /Human Interface/ADC_2
- U701 pad 25: (no net) -> /MCU/DATA0
- U701 pad 26: (no net) -> GND
- U701 pad 27: (no net) -> VDD
- U701 pad 28: (no net) -> /MCU/I2S3_LRCLK
- U701 pad 29: (no net) -> /Human Interface/CLK
- U701 pad 3: (no net) -> /MCU/LRCLK_MCU
- U701 pad 30: (no net) -> /Human Interface/ADC_3
- U701 pad 31: (no net) -> unconnected-(U701C-PA7-Pad31)
- U701 pad 32: (no net) -> /Human Interface/ADC_5
- U701 pad 33: (no net) -> /MCU/USB_B_VBUS_MCU
- U701 pad 34: (no net) -> /MCU/DATA1
- U701 pad 35: (no net) -> /MCU/DATA2
- U701 pad 36: (no net) -> /MCU/QUADSPI_CLK
- U701 pad 37: (no net) -> /MCU/QUADSPI_DATA_0
- U701 pad 38: (no net) -> /MCU/QUADSPI_DATA_1
- U701 pad 39: (no net) -> /MCU/QUADSPI_DATA_2
- U701 pad 4: (no net) -> /MCU/BCLK_MCU
- U701 pad 40: (no net) -> /MCU/QUADSPI_DATA_3
- U701 pad 41: (no net) -> /Audio IO/DACOUT1
- U701 pad 42: (no net) -> Net-(U701A-PE12)
- U701 pad 43: (no net) -> /Human Interface/serial_CLR
- U701 pad 44: (no net) -> /Human Interface/serial_data
- U701 pad 45: (no net) -> /Human Interface/register_CLK
- U701 pad 46: (no net) -> /MCU/DATA3
- U701 pad 47: (no net) -> /MCU/DATA4
- U701 pad 48: (no net) -> /MCU/VCAP1
- U701 pad 49: (no net) -> GND
- U701 pad 5: (no net) -> /Audio IO/ADCIN0
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
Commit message: Add even more component footprints and partnumbers
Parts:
- removed the C302 at (94.2, 122.5)
- removed the C302 at (252.3, 99.6)
- removed the C303 at (99.0, 56.8)
- removed the C303 at (91.8, 80.5)
- removed the C304 at (252.3, 105.4)
- removed the C304 at (91.8, 90.3)
- removed the C306 at (99.0, 60.8)
- removed the C306 at (94.2, 125.0)
- removed the C309 at (94.2, 127.5)
- removed the C309 at (252.3, 117.1)
- removed the C310 at (252.3, 123.0)
- removed the C310 at (94.2, 130.0)
- removed the C402 at (88.2, 122.5)
- removed the C402 at (345.5, 89.6)
- removed the C403 at (82.2, 56.8)
- removed the C403 at (75.0, 80.5)
- removed the C404 at (345.5, 95.5)
- removed the C404 at (75.0, 90.3)
- removed the C406 at (88.2, 125.0)
- removed the C406 at (82.2, 60.8)
- removed the C409 at (88.2, 127.5)
- removed the C409 at (345.5, 107.2)
- removed the C410 at (88.2, 130.0)
- removed the C410 at (345.5, 113.0)
- removed the C504 at (362.3, 83.8)
- removed the C504 at (75.3, 125.5)
- removed the C604 at (361.7, 58.6)
- removed the C604 at (84.2, 125.5)
- removed the C802 at (124.6, 133.8)
- removed the C802 at (297.8, 103.0)
- removed the C803 at (300.1, 93.9)
- removed the C803 at (124.6, 135.8)
- removed the C804 at (297.8, 106.0)
- removed the C804 at (124.6, 137.7)
- removed the C805 at (297.8, 109.0)
- removed the C805 at (124.6, 139.7)
- removed J703: Conn_ARM_SWD_TagConnect_TC2030, Connector:Tag-Connect_TC2030-IDC-FP_2x03_P1.27mm_Vertical
- added C302: 10uF/25V, Capacitor_SMD:CP_Elec_4x5.8, F.Cu at (166.1, 124.1)
- added C303: 100nF/50V, Capacitor_SMD:C_0805_2012Metric_Pad1.18x1.45mm_HandSolder, F.Cu at (172.2, 131.1)
- added C304: 10uF/25V, Capacitor_SMD:CP_Elec_4x5.8, F.Cu at (166.1, 129.9)
- added C306: 100nF/50V, Capacitor_SMD:C_0805_2012Metric_Pad1.18x1.45mm_HandSolder, F.Cu at (172.2, 137.1)
- added C309: 10uF/25V, Capacitor_SMD:CP_Elec_4x5.8, F.Cu at (166.1, 141.6)
- added C310: 10uF/25V, Capacitor_SMD:CP_Elec_4x5.8, F.Cu at (166.1, 147.5)
- added C402: 10uF/25V, Capacitor_SMD:CP_Elec_4x5.8, F.Cu at (186.3, 124.1)
- added C403: 100nF/50V, Capacitor_SMD:C_0805_2012Metric_Pad1.18x1.45mm_HandSolder, F.Cu at (192.4, 131.1)
- added C404: 10uF/25V, Capacitor_SMD:CP_Elec_4x5.8, F.Cu at (186.3, 129.9)
- added C406: 100nF/50V, Capacitor_SMD:C_0805_2012Metric_Pad1.18x1.45mm_HandSolder, F.Cu at (192.4, 137.1)
- added C409: 10uF/25V, Capacitor_SMD:CP_Elec_4x5.8, F.Cu at (186.3, 141.6)
- added C410: 10uF/25V, Capacitor_SMD:CP_Elec_4x5.8, F.Cu at (186.3, 147.5)
- added C504: 10uF/25V, Capacitor_SMD:CP_Elec_4x5.8, F.Cu at (147.1, 118.2)
- added C604: 10uF/25V, Capacitor_SMD:CP_Elec_4x5.8, F.Cu at (147.1, 155.3)
- added C802: 100nF/50V, Capacitor_SMD:C_0805_2012Metric_Pad1.18x1.45mm_HandSolder, F.Cu at (171.7, 90.7)
- added C803: 220uF, Capacitor_SMD:CP_Elec_4x5.8, F.Cu at (174.0, 81.6)
- added C804: 100nF/50V, Capacitor_SMD:C_0805_2012Metric_Pad1.18x1.45mm_HandSolder, F.Cu at (171.7, 93.7)
- added C805: 100nF/50V, Capacitor_SMD:C_0805_2012Metric_Pad1.18x1.45mm_HandSolder, F.Cu at (171.7, 96.7)
- added C916: 22uF/16V, Capacitor_SMD:CP_Elec_5x5.8, F.Cu at (98.5, 180.0)
- added C917: 100u/10V, Capacitor_SMD:CP_Elec_6.3x5.8, F.Cu at (88.8, 180.6)
- added C918: 100u/10V, Capacitor_SMD:CP_Elec_6.3x5.8, F.Cu at (88.8, 188.8)
- added D803: H5VL10B, LED_SMD:LED_0402_1005Metric_Pad0.77x0.64mm_HandSolder, F.Cu at (163.1, 104.5)
- added D804: H5VL10B, LED_SMD:LED_0402_1005Metric_Pad0.77x0.64mm_HandSolder, F.Cu at (163.1, 106.5)
- added J1301: PSG01550, Skrooter_footprints:psg01550, F.Cu at (240.2, 78.7)
- added J301: PSG01550, Skrooter_footprints:psg01550, F.Cu at (219.2, 102.8)
- added J401: PSG01550, Skrooter_footprints:psg01550, F.Cu at (219.2, 78.7)
- added RV1201: 10k/PTV112-4420A-B103, Skrooter_footprints:Potentiometer_Bourns_PTV09A-1_Dual_Vertical, F.Cu at (214.3, 48.7)
- added RV1301: 10k/PTV112-4420A-B103, Skrooter_footprints:Potentiometer_Bourns_PTV09A-1_Dual_Vertical, F.Cu at (236.1, 28.7)
- added RV1401: 10k/PTV09A-4020F-B103, Potentiometer_THT:Potentiometer_Bourns_PTV09A-1_Single_Vertical, F.Cu at (23.7, 50.4)
- added RV1402: 10k/PTV09A-4020F-B103, Potentiometer_THT:Potentiometer_Bourns_PTV09A-1_Single_Vertical, F.Cu at (23.7, 64.7)
- added RV1403: 10k/PTV09A-4020F-B103, Potentiometer_THT:Potentiometer_Bourns_PTV09A-1_Single_Vertical, F.Cu at (23.7, 79.1)
- added RV1404: 10k/PTV09A-4020F-B103, Potentiometer_THT:Potentiometer_Bourns_PTV09A-1_Single_Vertical, F.Cu at (23.7, 93.4)
- added RV1405: 10k/PTV09A-4020F-B103, Potentiometer_THT:Potentiometer_Bourns_PTV09A-1_Single_Vertical, F.Cu at (23.7, 107.8)
- added RV1406: 10k/PTV09A-4020F-B103, Potentiometer_THT:Potentiometer_Bourns_PTV09A-1_Single_Vertical, F.Cu at (23.7, 122.1)
- added RV1407: 10k/PTV09A-4020F-B103, Potentiometer_THT:Potentiometer_Bourns_PTV09A-1_Single_Vertical, F.Cu at (39.2, 50.4)
- added RV1408: 10k/PTV09A-4020F-B103, Potentiometer_THT:Potentiometer_Bourns_PTV09A-1_Single_Vertical, F.Cu at (39.2, 64.7)
- added RV1409: 10k/ PTA6043-2015DPB103, Potentiometer_THT:Potentiometer_Bourns_PTA6043_Single_Slide, F.Cu at (24.3, 20.8)
- added RV1410: 10k/PTV09A-4020F-B103, Potentiometer_THT:Potentiometer_Bourns_PTV09A-1_Single_Vertical, F.Cu at (39.2, 79.1)
- added RV1411: 10k/PTV09A-4020F-B103, Potentiometer_THT:Potentiometer_Bourns_PTV09A-1_Single_Vertical, F.Cu at (39.2, 93.4)
- added RV1412: 10k/PTV09A-4020F-B103, Potentiometer_THT:Potentiometer_Bourns_PTV09A-1_Single_Vertical, F.Cu at (39.2, 107.8)
- added RV1413: 10k/PTV09A-4020F-B103, Potentiometer_THT:Potentiometer_Bourns_PTV09A-1_Single_Vertical, F.Cu at (39.2, 122.1)
- added RV1414: 10k/PTV09A-4020F-B103, Potentiometer_THT:Potentiometer_Bourns_PTV09A-1_Single_Vertical, F.Cu at (54.6, 50.4)
- added RV1415: 10k/PTV09A-4020F-B103, Potentiometer_THT:Potentiometer_Bourns_PTV09A-1_Single_Vertical, F.Cu at (54.6, 64.7)
- added RV1416: 10k/PTV09A-4020F-B103, Potentiometer_THT:Potentiometer_Bourns_PTV09A-1_Single_Vertical, F.Cu at (54.6, 79.1)
- added RV1417: 10k/PTV09A-4020F-B103, Potentiometer_THT:Potentiometer_Bourns_PTV09A-1_Single_Vertical, F.Cu at (54.6, 93.4)
- added RV1418: 10k/PTV09A-4020F-B103, Potentiometer_THT:Potentiometer_Bourns_PTV09A-1_Single_Vertical, F.Cu at (54.6, 107.8)
- added RV1419: 10k/PTV09A-4020F-B103, Potentiometer_THT:Potentiometer_Bourns_PTV09A-1_Single_Vertical, F.Cu at (54.6, 122.1)
- added RV1420: 10k/PTV09A-4020F-B103, Potentiometer_THT:Potentiometer_Bourns_PTV09A-1_Single_Vertical, F.Cu at (70.1, 50.4)
- added RV1421: 10k/PTV09A-4020F-B103, Potentiometer_THT:Potentiometer_Bourns_PTV09A-1_Single_Vertical, F.Cu at (70.1, 64.7)
- added RV1422: 10k/PTV09A-4020F-B103, Potentiometer_THT:Potentiometer_Bourns_PTV09A-1_Single_Vertical, F.Cu at (70.1, 79.1)
- added RV1423: 10k/PTV09A-4020F-B103, Potentiometer_THT:Potentiometer_Bourns_PTV09A-1_Single_Vertical, F.Cu at (70.1, 93.4)
- added RV1424: 10k/ PTA6043-2015DPB103, Potentiometer_THT:Potentiometer_Bourns_PTA6043_Single_Slide, F.Cu at (24.3, 32.9)
- added RV301: 10k/PTV112-4420A-B103, Skrooter_footprints:Potentiometer_Bourns_PTV09A-1_Dual_Vertical, F.Cu at (236.1, 48.7)
- added RV401: 10k/PTV112-4420A-B103, Skrooter_footprints:Potentiometer_Bourns_PTV09A-1_Dual_Vertical, F.Cu at (214.3, 28.7)
- added SW1801: ~, Button_Switch_SMD:SW_Push_1P1T_XKB_TS-1187A, F.Cu at (105.8, 71.9)
- added SW1802: ~, Button_Switch_SMD:SW_Push_1P1T_XKB_TS-1187A, F.Cu at (105.8, 78.6)
- added SW1803: ~, Button_Switch_SMD:SW_Push_1P1T_XKB_TS-1187A, F.Cu at (105.8, 85.2)
- added SW1804: ~, Button_Switch_SMD:SW_Push_1P1T_XKB_TS-1187A, F.Cu at (105.8, 91.9)
- added SW1805: ~, Button_Switch_SMD:SW_Push_1P1T_XKB_TS-1187A, F.Cu at (114.4, 71.9)
- added SW1806: ~, Button_Switch_SMD:SW_Push_1P1T_XKB_TS-1187A, F.Cu at (114.4, 78.6)
- added SW1807: ~, Button_Switch_SMD:SW_Push_1P1T_XKB_TS-1187A, F.Cu at (114.4, 85.2)
- added SW1808: ~, Button_Switch_SMD:SW_Push_1P1T_XKB_TS-1187A, F.Cu at (114.4, 91.9)
- added SW1809: ~, Button_Switch_SMD:SW_Push_1P1T_XKB_TS-1187A, F.Cu at (122.9, 71.9)
- added SW1810: ~, Button_Switch_SMD:SW_Push_1P1T_XKB_TS-1187A, F.Cu at (122.9, 78.6)
- added SW1811: ~, Button_Switch_SMD:SW_Push_1P1T_XKB_TS-1187A, F.Cu at (122.9, 85.2)
- added SW1812: ~, Button_Switch_SMD:SW_Push_1P1T_XKB_TS-1187A, F.Cu at (122.9, 91.9)
- added SW1813: ~, Button_Switch_SMD:SW_Push_1P1T_XKB_TS-1187A, F.Cu at (131.5, 71.9)
- added SW1814: ~, Button_Switch_SMD:SW_Push_1P1T_XKB_TS-1187A, F.Cu at (131.5, 78.6)
- added SW1815: ~, Button_Switch_SMD:SW_Push_1P1T_XKB_TS-1187A, F.Cu at (131.5, 85.2)
- added SW1816: ~, Button_Switch_SMD:SW_Push_1P1T_XKB_TS-1187A, F.Cu at (131.5, 91.9)
- added U1101: NE5532, Package_SO:SOIC-8_3.9x4.9mm_P1.27mm, F.Cu at (191.4, 98.7)
- added U1201: NE5532, Package_SO:SOIC-8_3.9x4.9mm_P1.27mm, F.Cu at (170.7, 19.7)
- added U1202: NE5532, Package_SO:SOIC-8_3.9x4.9mm_P1.27mm, F.Cu at (170.7, 26.2)
- added U1203: TDA2822D, Package_SO:SOP-8_3.9x4.9mm_P1.27mm, F.Cu at (170.7, 32.6)
- added U1301: NE5532, Package_SO:SOIC-8_3.9x4.9mm_P1.27mm, F.Cu at (120.7, 160.3)
- added U1302: NE5532, Package_SO:SOIC-8_3.9x4.9mm_P1.27mm, F.Cu at (120.7, 166.7)
- added U1303: NE5532, Package_SO:SOIC-8_3.9x4.9mm_P1.27mm, F.Cu at (120.7, 173.2)
- added U502: NE5532, Package_SO:SOIC-8_3.9x4.9mm_P1.27mm, F.Cu at (155.2, 136.6)
- added U602: NE5532, Package_SO:SOIC-8_3.9x4.9mm_P1.27mm, F.Cu at (155.2, 173.7)
- C1001, C1002, C1102, C1211, C1213, C1216, C1217, C1303, C1306, C1307, C1501, C1601, C1701, C1801, C1802, C1803, C1804, C1805, C1806, C1807, C1808, C1809, C1810, C1811, C1812, C1813, C1814, C1815, C1816, C1817, C2001, C2002, C2003, C2004, C2005, C305, C308, C405, C408, C501, C503, C506, C601, C603, C606, C705, C706, C707, C708, C709, C710, C711, C713, C715, C801, C912, C915: value 100nF/16V -> 100nF/50V; footprint Capacitor_SMD:C_0805_2012Metric -> Capacitor_SMD:C_0805_2012Metric_Pad1.18x1.45mm_HandSolder
- C1205, C1206, C1308, C1309, C1312, C1313, C502, C509, C510, C602, C609, C610, C701, C702, C703, C704, C712, C714, C716, C806, C807, C904, C905, C906, C907, C911: footprint Capacitor_SMD:C_0805_2012Metric -> Capacitor_SMD:C_0805_2012Metric_Pad1.18x1.45mm_HandSolder
- C201: footprint Capacitor_SMD:C_0603_1608Metric -> Capacitor_SMD:C_0603_1608Metric_Pad1.08x0.95mm_HandSolder
- C902, C903, C908, C909, C910, C913, C914: value 470uF/10V -> 4.7uF/25V; footprint Capacitor_SMD:CP_Elec_6.3x7.7 -> Capacitor_SMD:C_0805_2012Metric_Pad1.18x1.45mm_HandSolder
- L901, L902: footprint SkrooterFootprints:MSCD43 -> Skrooter_footprints:MSCD43
- R1101, R1102, R1201, R1202, R1207, R1208, R1211, R1212, R1301, R1302, R1307, R1308, R1317, R1318, R1801, R1802, R1803, R1804, R1805, R1810, R1811, R1812, R1813, R1818, R1819, R1820, R1821, R1826, R1827, R1828, R1832, R201, R202, R301, R302, R401, R402, R501, R502, R505, R506, R601, R602, R605, R606, R701, R702, R703, R704, R705, R706, R707, R708, R709, R801, R802, R807, R811, R812, R906, R908: footprint Resistor_SMD:R_0805_2012Metric -> Resistor_SMD:R_0805_2012Metric_Pad1.20x1.40mm_HandSolder
- U701: footprint SkrooterFootprints:LQFP100-14x14mm -> Skrooter_footprints:LQFP100-14x14mm
- U801: value USBLC6-4SC6 -> SRV05-4
- moved F902 286.1 mm to (72.8, 160.4)
- moved C912 280.0 mm to (69.7, 145.4)
- moved C915 280.0 mm to (69.7, 148.4)
- moved C907 279.7 mm to (69.7, 139.4)
- moved C901 274.5 mm to (80.5, 138.2)
- moved R908 270.4 mm to (78.9, 145.5)
- moved J1001 247.5 mm to (33.1, 141.7)
- moved J1002 247.5 mm to (33.1, 161.7)
- moved J1003 247.5 mm to (33.1, 181.7)
- moved C605 235.4 mm to (147.1, 161.2)
- moved C602 234.2 mm to (153.2, 156.9)
- moved R605 233.8 mm to (157.7, 159.8)
- moved R606 233.8 mm to (157.7, 162.7)
- moved U1701 226.8 mm to (178.0, 180.4)
- moved C1701 226.8 mm to (184.4, 176.1)
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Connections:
- net IN renamed /POWER/VBUS_{fused}
- J1201 pad RN: (no net) -> unconnected-(J1201-PadRN)
- J1201 pad TN: (no net) -> unconnected-(J1201-PadTN)
- U701 pad 90: /MCU/NJTRST -> unconnected-(U701C-PB4-Pad90)
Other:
- board size 100 x 100 mm -> 13 x 1.4 mm
